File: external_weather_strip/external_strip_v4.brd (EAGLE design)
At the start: 40 x 30 mm, 37 parts, among them IC1 BMP280, Q1 32.768kHz, U2 SHT21, U3 ML8511-UV-SENSORSMD, U4 MCP3425, U5 LM4132-2.048V, U6 BNO055A, U7 AS3935

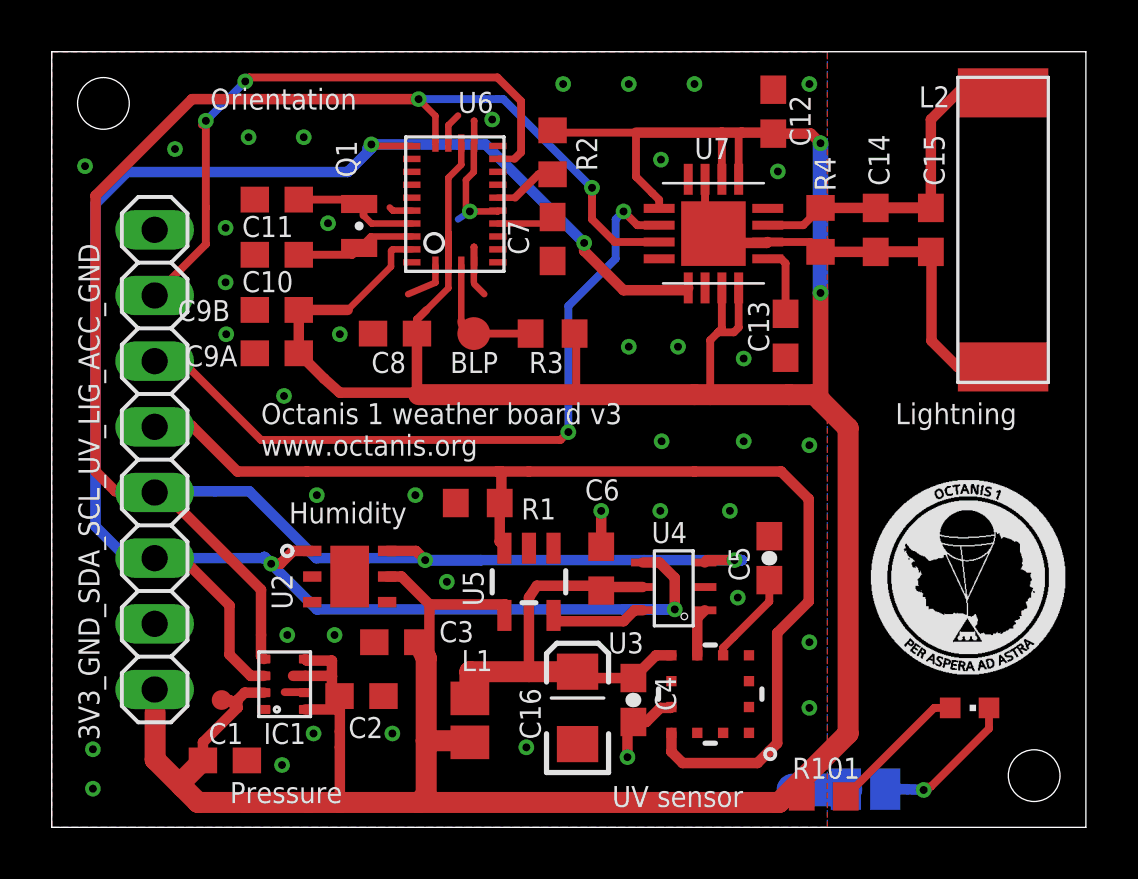
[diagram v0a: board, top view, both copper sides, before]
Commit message: finalized silkscreen, generated Gerber files for EPS v2; replaced UV sensor in weather board, generated gerber files for v4
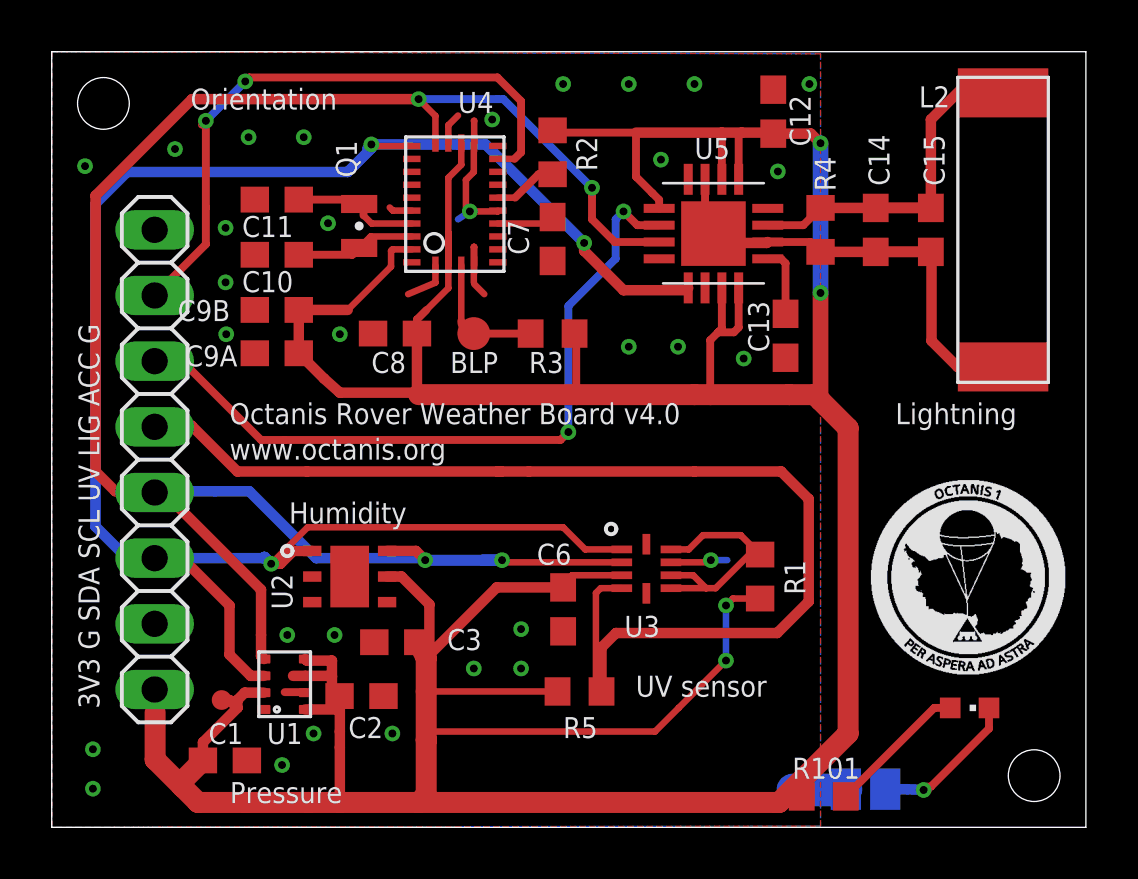
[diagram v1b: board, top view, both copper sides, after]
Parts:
- removed C16: 10uF, SparkFun-Retired:EIA3216
- removed C4: 100n, SparkFun-Capacitors:0603-CAP
- removed C5: 1n, SparkFun-Capacitors:0603-CAP
- removed L1: (no value), dp_devices:FB603
- removed U6: BNO055A, BNO055:BNO055
- removed U7: AS3935, AS3935:16LDMLPQ
- added R5: 5k1, rcl:R0603
- R1: device resistor:R0603 -> rcl:R0603
- U3: value ML8511-UV-SENSORSMD -> SI1133; device SparkFun-Sensors:ML8511 -> Octanis1:DFN2X2
- U4: value MCP3425 -> BNO055A; device phMeter:SOT-23-6 -> BNO055:BNO055
- U5: value LM4132-2.048V -> AS3935; device SparkFun:SOT23-5 -> AS3935:16LDMLPQ
- moved U4 18.7 mm to (13.6, 27.1), turned to 180 degrees
- moved U5 15.2 mm to (23.6, 26.0)
- moved R1 11.3 mm to (25.4, 12.7), turned to 270 degrees
- moved U3 5.44 mm to (21.0, 13.0)
- moved C6 2.16 mm to (17.8, 11.4), turned to 270 degrees
- renumbered IC1 to U1
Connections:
- removed net AVCC: C16.A, C4.1, C6.1, L1.2, U3.7, U4.VDD
- removed net N$1: U3.8, U4.VIN+
- removed net N$3: C5.1, U3.9
- removed net N$6: U4.VIN-, U5.5
- removed net UV_EN: JP2.5, R1.1, U3.4, U5.3
- new net N$9: R1.1, U3.P$6, U3.P$7, U3.P$9
- new net UV_IRQ: JP2.5, R5.2, U3.P$4
- net +3V3: now also C6.1, R1.2, R5.1, U3.P$3, U4.17, U4.28, U4.3, U5.15, U5.16, U5.5, U5.6, U5.9; no longer L1.1, U5.4, U6.17, U6.28, U6.3, U7.15, U7.16, U7.5, U7.6, U7.9
- net ACCEL_IRQ: now also U4.14; no longer U6.14
- net ACCEL_N_BOOTLD: now also U4.4; no longer U6.4
- net ACCEL_N_RST: now also U4.11; no longer U6.11
- net GND: now also U3.P$8, U4.10, U4.15, U4.16, U4.18, U4.2, U4.25, U4.5, U4.6, U5.4, U5.7, U5.EXP; no longer C16.C, C4.2, C5.2, R1.2, U3.5, U4.VSS, U6.10, U6.15, U6.16, U6.18, U6.2, U6.25, U6.5, U6.6, U7.2, U7.4, U7.7, U7.EXP
- net LIGHTNING_IRQ: now also U5.10; no longer U7.10
- net N$18: now also U4.9; no longer U6.9
- net N$19: now also U4.27; no longer U6.27
- net N$2: now also U5.1; no longer U7.1
- net N$5: now also U5.3; no longer U7.3
- net N$73: now also U4.26; no longer U6.26
- net SCL: now also U3.P$2, U4.19, U5.11; no longer U4.SCL, U6.19, U7.11
- net SDA: now also U3.P$1, U4.20, U5.13; no longer U4.SDA, U6.20, U7.13
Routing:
- net UV_IRQ: track 0.00 -> 45.9 mm
- net UV_EN: track 45.1 -> 0.00 mm
- net +3V3: track 163.3 -> 188.4 mm, vias 2 -> 4
- net AVCC: track 17.2 -> 0.00 mm
- net N$9: track 0.00 -> 9.54 mm
- net SDA: track 78.7 -> 72.2 mm, vias 4 -> 3
- net N$6: track 3.72 -> 0.00 mm
- net N$3: track 3.65 -> 0.00 mm
- net SCL: track 80.2 -> 77.3 mm
- net GND: track 39.3 -> 36.9 mm, vias 42 -> 31
- net N$1: track 1.86 -> 0.00 mm
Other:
- board text added: "3V3 G SDA SCL UV LIG ACC G"
- board text added: "Octanis Rover Weather Board v4.0"
- board text removed: "3V3_GND_SDA_SCL_UV_LIG_ACC_GND"
- board text removed: "Octanis 1 weather board v3"
- board text removed: "U3"
- board text removed: "U4"
